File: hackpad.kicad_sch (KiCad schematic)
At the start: 0 parts

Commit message: Add KiCad schematic, project and prefs files
Add hackpad.kicad_sch (complete schematic containing component symbols, instances, wires and junctions for push switches, diodes and a rotary encoder), populate hackpad.kicad_pro with project metadata, top-level sheet reference and net/ERC/BOM/settings, and add hackpad.kicad_prl with editor/view preferences. Also normalizes the schematic UUID formatting. These files establish the hackpad KiCad project configuration and schematic content.
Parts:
- added D1, D10, D11, D12, D2, D3, D4, D5, D6, D7, D8, D9: 1N4148, Diode_THT:D_DO-35_SOD27_P7.62mm_Horizontal, symbol Diode:1N4148
- added SW1, SW10, SW11, SW12, SW2, SW3, SW4, SW5, SW6, SW7, SW8, SW9: SW_Push, symbol Switch:SW_Push
- added SW13: RotaryEncoder_Switch, symbol Device:RotaryEncoder_Switch
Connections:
- new net: SW1.1, SW4.1, SW7.1
- new net: D4.2 (A), SW4.2
- new net: D7.2 (A), SW7.2
- new net: SW10.1, SW11.1, SW12.1
- new net: D12.2 (A), SW12.2
- new net: D1.1 (K), D10.1 (K), D2.1 (K), D3.1 (K)
- new net: D3.2 (A), SW3.2
- new net: SW2.1, SW5.1, SW8.1
- new net: D5.2 (A), SW5.2
- new net: D1.2 (A), SW1.2
- new net: SW3.1, SW6.1, SW9.1
- new net: D6.2 (A), SW6.2
- new net: D11.2 (A), SW11.2
- new net: D2.2 (A), SW2.2
- new net: D8.2 (A), SW8.2
- new net: D10.2 (A), SW10.2
- new net: D9.2 (A), SW9.2

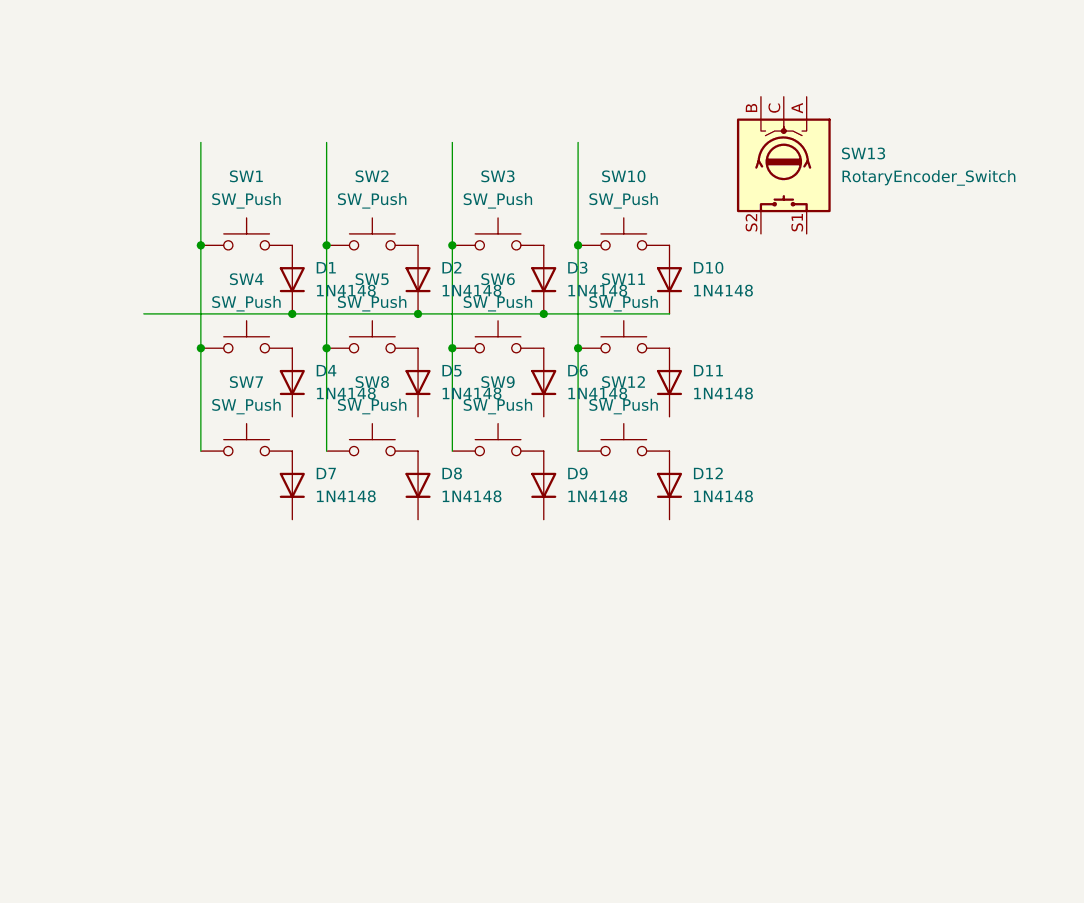
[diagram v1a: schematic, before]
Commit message: Update KiCad schematic, project settings
Add and update KiCad project and schematic data: populate net inspector columns; add extensive board design_settings (DRC rules, teardrop/tearing, track/tuning, pad/zone defaults); change annotation sort order and used_designators. In schematic: add many junctions, wires, labels and symbols; add/set footprints, datasheets and simulation properties for diodes; add new switch/encoder symbols; and renumber/rename multiple component references (SWx, Dx) and adjust positions/UUIDs. These changes update the board rules and reorganize schematic elements/refs for the current design.
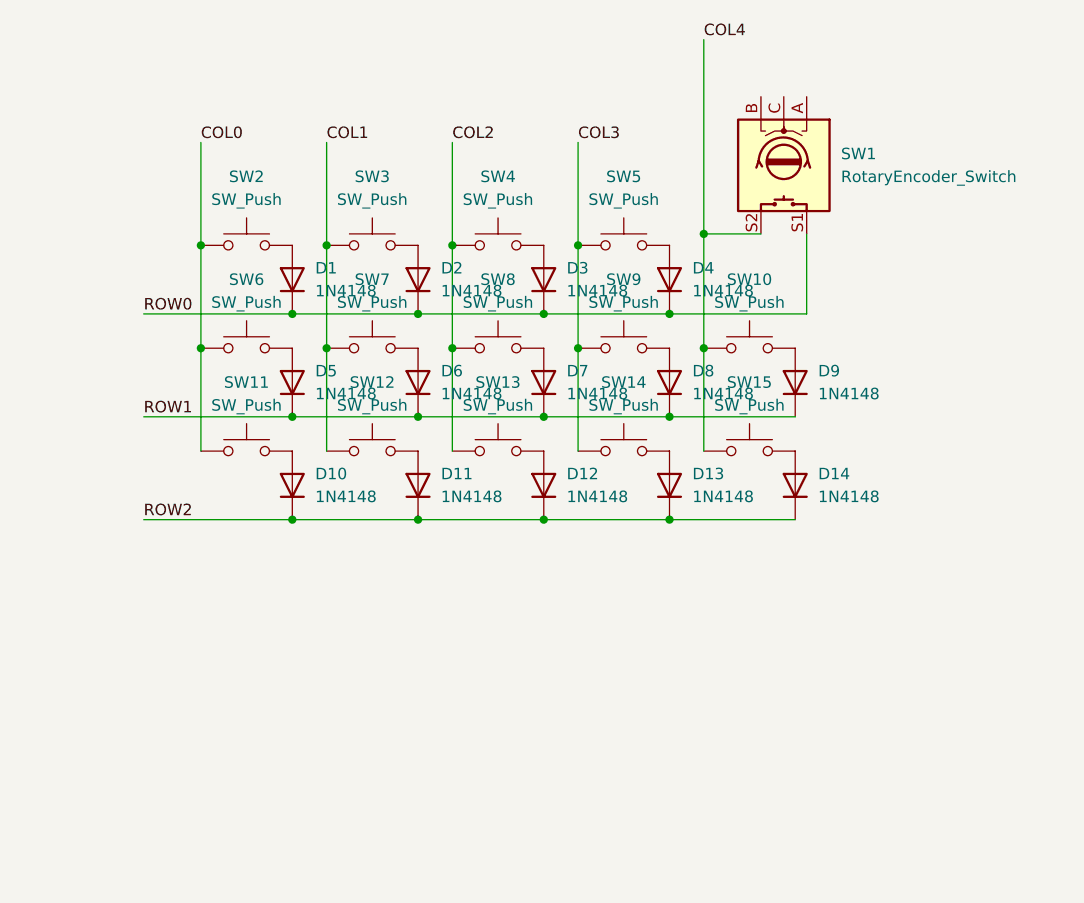
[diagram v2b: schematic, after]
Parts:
- added D14, D9: 1N4148, Diode_THT:D_DO-35_SOD27_P7.62mm_Horizontal, symbol Diode:1N4148
- added SW10, SW15: SW_Push, PCM_marbastlib-various:SW_Push_1P1T-NO_Horizontal_C&K_NANOT_240_BP, symbol Switch:SW_Push
- SW1: renamed from SW13; footprint (none) -> Rotary_Encoder:RotaryEncoder_Alps_EC11E-Switch_Vertical_H20mm
- SW11: renamed from SW7; footprint (none) -> PCM_marbastlib-various:SW_Push_1P1T-NO_Horizontal_C&K_NANOT_240_BP
- SW12: renamed from SW8; footprint (none) -> PCM_marbastlib-various:SW_Push_1P1T-NO_Horizontal_C&K_NANOT_240_BP
- SW13: renamed from SW9; footprint (none) -> PCM_marbastlib-various:SW_Push_1P1T-NO_Horizontal_C&K_NANOT_240_BP
- SW14: renamed from SW12; footprint (none) -> PCM_marbastlib-various:SW_Push_1P1T-NO_Horizontal_C&K_NANOT_240_BP
- SW2: renamed from SW1; footprint (none) -> PCM_marbastlib-various:SW_Push_1P1T-NO_Horizontal_C&K_NANOT_240_BP
- SW3: renamed from SW2; footprint (none) -> PCM_marbastlib-various:SW_Push_1P1T-NO_Horizontal_C&K_NANOT_240_BP
- SW4: renamed from SW3; footprint (none) -> PCM_marbastlib-various:SW_Push_1P1T-NO_Horizontal_C&K_NANOT_240_BP
- SW5: renamed from SW10; footprint (none) -> PCM_marbastlib-various:SW_Push_1P1T-NO_Horizontal_C&K_NANOT_240_BP
- SW6: renamed from SW4; footprint (none) -> PCM_marbastlib-various:SW_Push_1P1T-NO_Horizontal_C&K_NANOT_240_BP
- SW7: renamed from SW5; footprint (none) -> PCM_marbastlib-various:SW_Push_1P1T-NO_Horizontal_C&K_NANOT_240_BP
- SW8: renamed from SW6; footprint (none) -> PCM_marbastlib-various:SW_Push_1P1T-NO_Horizontal_C&K_NANOT_240_BP
- SW9: renamed from SW11; footprint (none) -> PCM_marbastlib-various:SW_Push_1P1T-NO_Horizontal_C&K_NANOT_240_BP
- renumbered D7 to D10, D8 to D11, D9 to D12, D12 to D13, D10 to D4, D4 to D5, D5 to D6, D6 to D7, D11 to D8
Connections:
- net COL0: now reaches SW11.1, SW2.1, SW6.1
- net ROW0: now reaches SW1.S1
- net ROW0: now also D1.1 (K), D2.1 (K), D3.1 (K), D4.1 (K)
- net COL4: now reaches SW1.S2
- net COL4: now also SW10.1, SW15.1
- net COL3: now reaches SW14.1, SW5.1, SW9.1
- net ROW2: now reaches D13.1 (K)
- net ROW2: now also D10.1 (K), D11.1 (K), D12.1 (K), D14.1 (K)
- net COL1: now reaches SW12.1, SW3.1, SW7.1
- net COL2: now reaches SW13.1, SW4.1, SW8.1
- net ROW1: now reaches D8.1 (K)
- net ROW1: now also D5.1 (K), D6.1 (K), D7.1 (K), D9.1 (K)
- new net: D14.2 (A), SW15.2
- new net: D9.2 (A), SW10.2

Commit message: Made some amazing progress and finished pcb
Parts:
- removed D4, D8: 1N4148, Diode_THT:D_DO-35_SOD27_P7.62mm_Horizontal, symbol Diode:1N4148
- removed SW5, SW9: SW_Push, PCM_marbastlib-various:SW_Push_1P1T-NO_Horizontal_C&K_NANOT_240_BP, symbol Switch:SW_Push
- added D1, D14, D15, D16: 1N4148, Diode_THT:D_DO-35_SOD27_P7.62mm_Horizontal, symbol Diode:1N4148
- added SW13, SW15, SW16: SW_Push, PCM_marbastlib-mx:SW_MX_1u, symbol Switch:SW_Push
- added U1: MOUDLE-SEEEDUINO-XIAO, hackclub_lib:XIAO-Generic-Hybrid-14P-2.54-21X17.8MM, symbol hackclub_lib:MOUDLE-SEEEDUINO-XIAO
- SW10: renamed from SW12; footprint PCM_marbastlib-various:SW_Push_1P1T-NO_Horizontal_C&K_NANOT_240_BP -> PCM_marbastlib-mx:SW_MX_1u
- SW11: renamed from SW13; footprint PCM_marbastlib-various:SW_Push_1P1T-NO_Horizontal_C&K_NANOT_240_BP -> PCM_marbastlib-mx:SW_MX_1u
- SW12: renamed from SW15; footprint PCM_marbastlib-various:SW_Push_1P1T-NO_Horizontal_C&K_NANOT_240_BP -> PCM_marbastlib-mx:SW_MX_1u
- SW14, SW2, SW3, SW4: footprint PCM_marbastlib-various:SW_Push_1P1T-NO_Horizontal_C&K_NANOT_240_BP -> PCM_marbastlib-mx:SW_MX_1u
- SW5: renamed from SW6; footprint PCM_marbastlib-various:SW_Push_1P1T-NO_Horizontal_C&K_NANOT_240_BP -> PCM_marbastlib-mx:SW_MX_1u
- SW6: renamed from SW7; footprint PCM_marbastlib-various:SW_Push_1P1T-NO_Horizontal_C&K_NANOT_240_BP -> PCM_marbastlib-mx:SW_MX_1u
- SW7: renamed from SW8; footprint PCM_marbastlib-various:SW_Push_1P1T-NO_Horizontal_C&K_NANOT_240_BP -> PCM_marbastlib-mx:SW_MX_1u
- SW8: renamed from SW10; footprint PCM_marbastlib-various:SW_Push_1P1T-NO_Horizontal_C&K_NANOT_240_BP -> PCM_marbastlib-mx:SW_MX_1u
- SW9: renamed from SW11; footprint PCM_marbastlib-various:SW_Push_1P1T-NO_Horizontal_C&K_NANOT_240_BP -> PCM_marbastlib-mx:SW_MX_1u
- renumbered D11 to D10, D12 to D11, D14 to D12, D1 to D2, D2 to D3, D3 to D4, D9 to D8, D10 to D9
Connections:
- net COL4 is gone; now on net COL3: SW1.S2, SW12.1, SW8.1
- net COL0: now also SW13.1, U1.5 (PA8_A4_D4_SDA)
- net COL1: now also SW14.1, U1.6 (PA9_A5_D5_SCL)
- net COL2: now also SW15.1, U1.7 (PB08_A6_D6_TX)
- net COL3: now also SW16.1, U1.8 (PB09_A7_D7_RX); no longer SW14.1
- net ROW0: now also D1.1 (K), U1.1 (PA02_A0_D0); no longer SW1.S1
- net ROW1: now also U1.2 (PA4_A1_D1)
- net ROW2: now also U1.3 (PA10_A2_D2); no longer D13.1 (K)
- net POT1: now reaches SW1.A
- net POT1: now also U1.10 (PA5_A9_D9_MISO)
- net POT0: now reaches SW1.B
- net POT0: now also U1.9 (PA7_A8_D8_SCK)
- net GND: now reaches SW1.C
- net at SW14.2: now also D14.2 (A); no longer D13.2 (A)
- new net: D15.2 (A), SW15.2
- new net: D16.2 (A), SW16.2
- new net: D13.2 (A), SW13.2
- new net: D1.2 (A), SW1.S1
- new net ROW3: D13.1 (K), D14.1 (K), D15.1 (K), D16.1 (K), U1.4 (PA11_A3_D3)
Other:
- moved on the sheet: D12, D8, SW1, SW12, SW8
